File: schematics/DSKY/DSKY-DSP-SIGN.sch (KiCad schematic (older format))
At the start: 10 parts, among them U17 74LS32, U38 74LS74, U39 74LS74, U41 74LS74, U42 74LS04, U44 74LS08, U45 74LS04, U48 74LS00, U60 74LS10, U8 74LS10

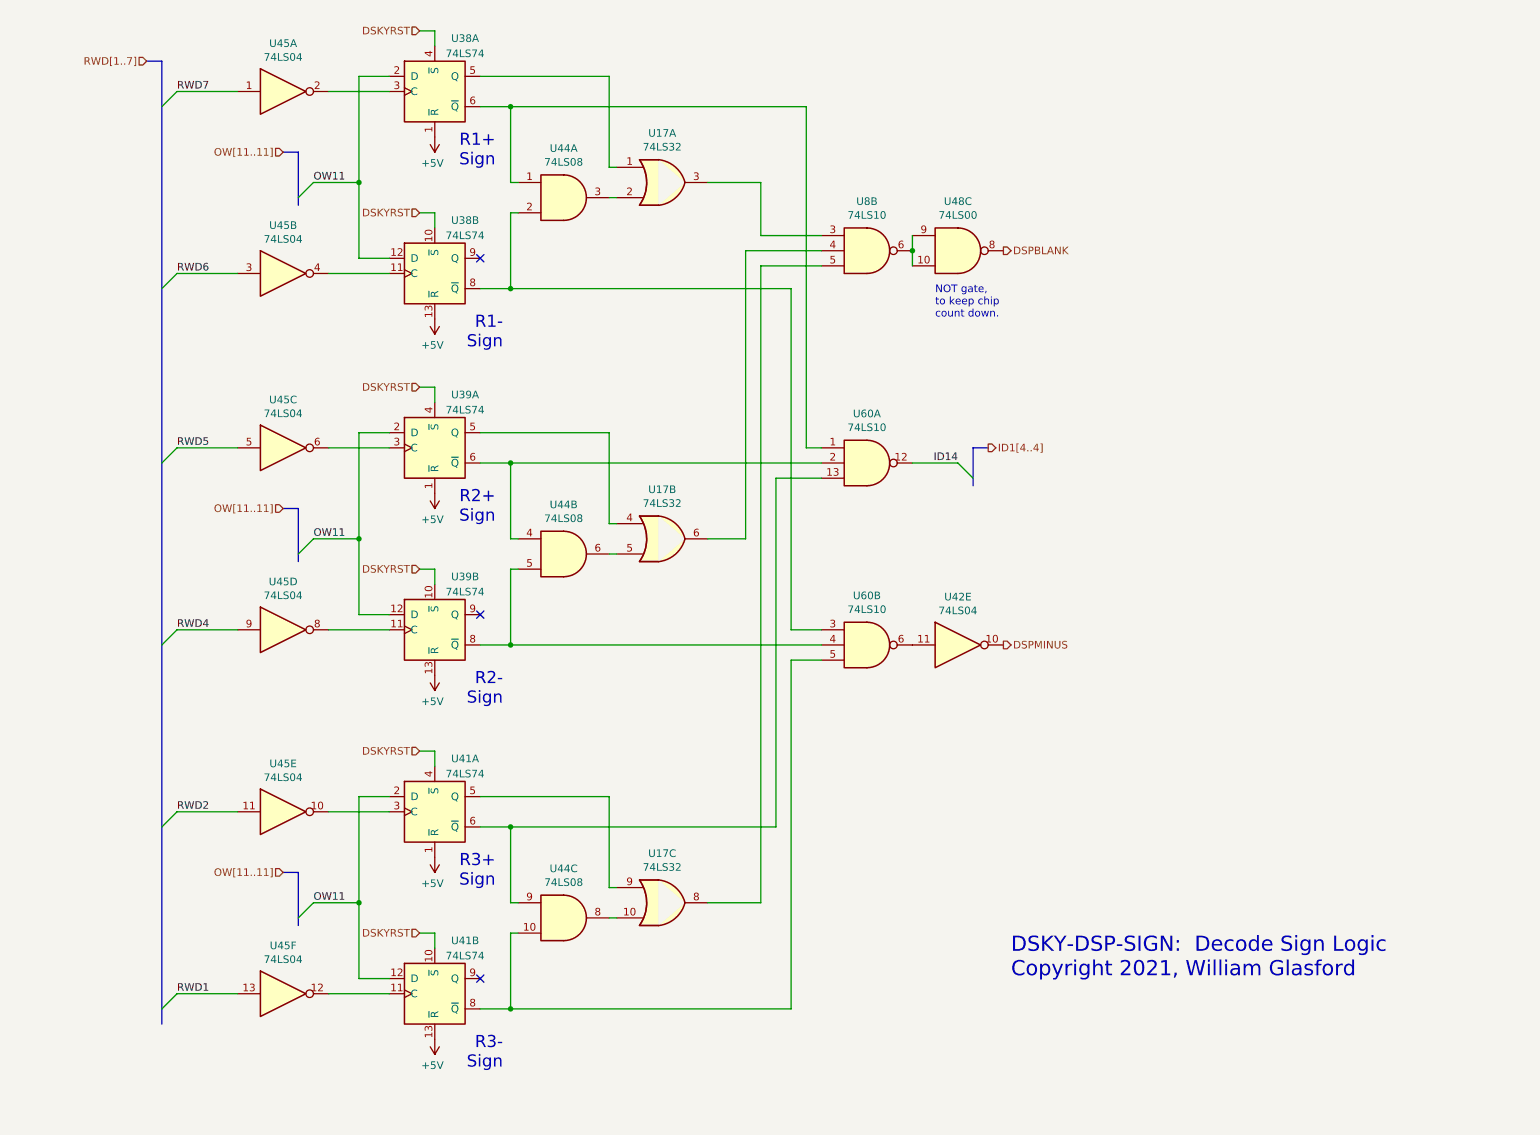
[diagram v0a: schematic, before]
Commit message: Overhauled the handling of the sign characters.
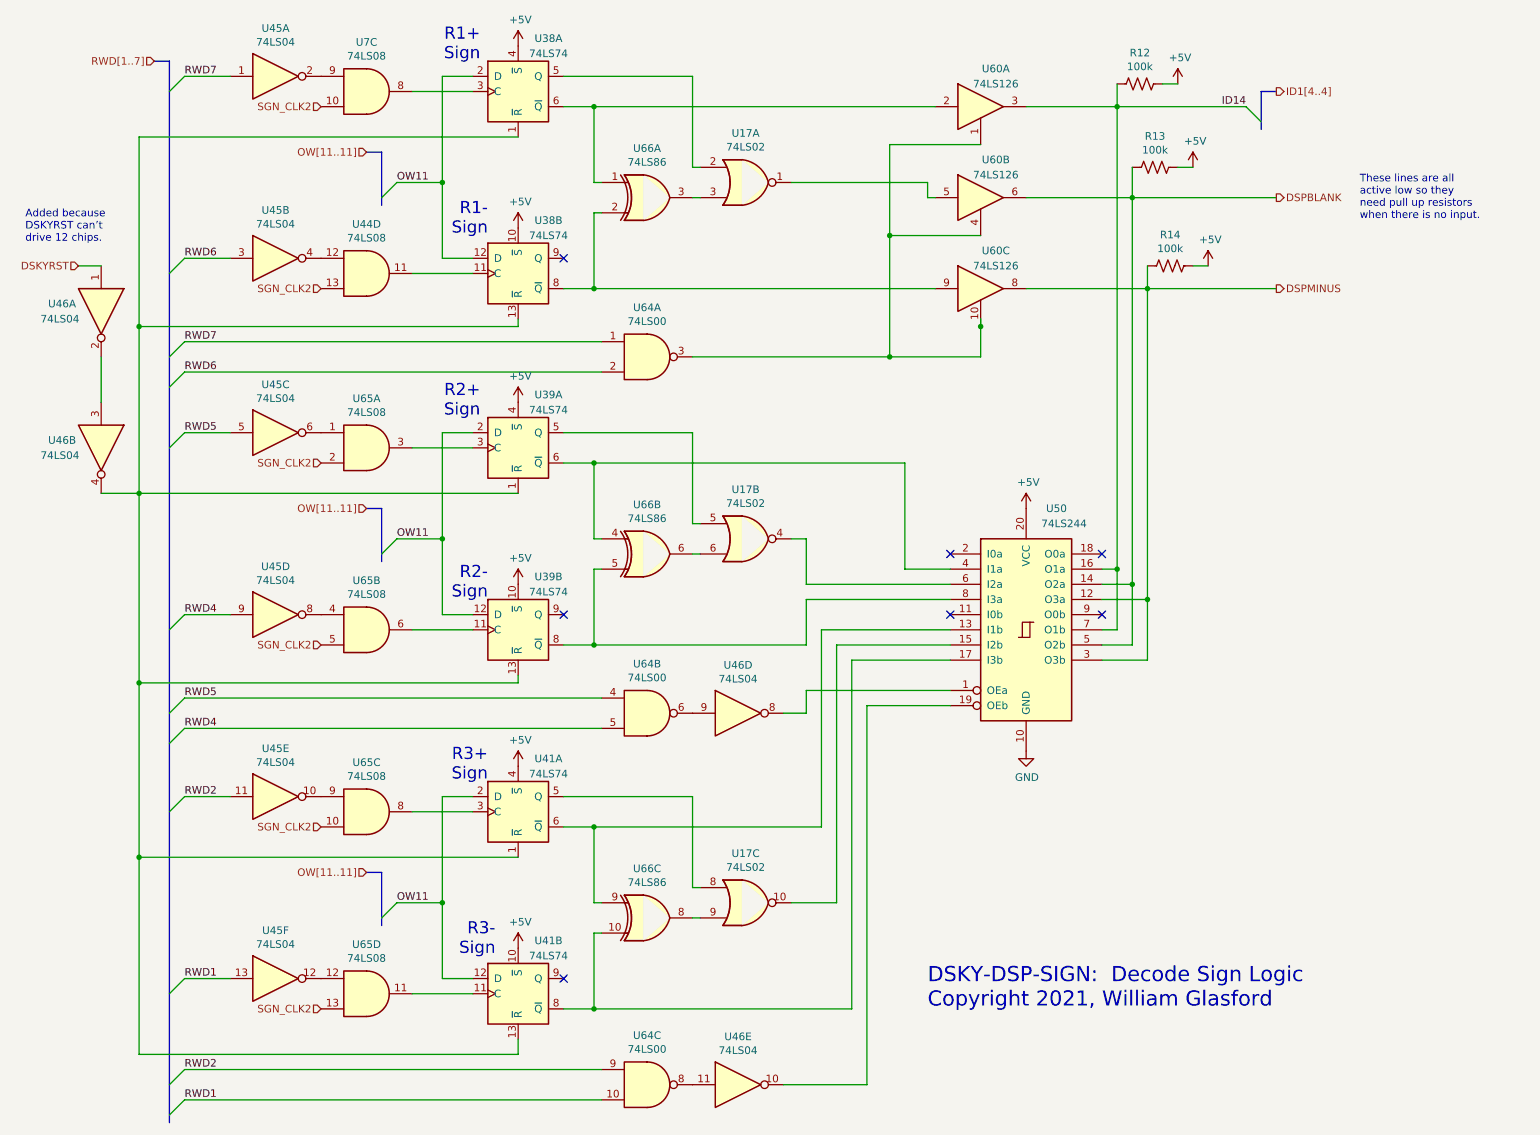
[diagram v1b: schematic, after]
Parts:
- removed U17: 74LS32, symbol 74xx:74LS32
- removed U42: 74LS04, symbol 74xx:74LS04
- removed U44: 74LS08, symbol 74xx:74LS08
- removed U48: 74LS00, symbol 74xx:74LS00
- removed U60, U8: 74LS10, symbol 74xx:74LS10
- added R12, R13, R14: 100k, symbol Device:R_US
- added U17: 74LS02, symbol 74xx:74LS02
- added U44, U65, U7: 74LS08, symbol 74xx:74LS08
- added U46: 74LS04, symbol 74xx:74LS04
- added U50: 74LS244, symbol 74xx:74LS244
- added U60: 74LS126, symbol 74xx:74LS126
- added U64: 74LS00, symbol 74xx:74LS00
- added U66: 74LS86, symbol 74xx:74LS86
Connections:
- net +5V: now also U38.10 (~S), U38.4 (~S), U39.10 (~S), U39.4 (~S), U41.10 (~S), U41.4 (~S), R12.1, R13.1, R14.1, U50.20 (VCC); no longer U38.1 (~R), U38.13 (~R), U39.1 (~R), U39.13 (~R), U41.1 (~R), U41.13 (~R)
- net DSKYRST: now also U46.1; no longer U38.10 (~S), U38.4 (~S), U39.10 (~S), U39.4 (~S), U41.10 (~S), U41.4 (~S)
- net DSPBLANK: now also R13.2, U50.14 (O2a), U50.5 (O2b), U60.6
- net DSPMINUS: now also R14.2, U50.12 (O3a), U50.3 (O3b), U60.8
- net ID14: now also R12.2, U50.16 (O1a), U50.7 (O1b), U60.3
- net RWD1: now also U64.10
- net RWD2: now also U64.9
- net RWD4: now also U64.5
- net RWD5: now also U64.4
- net RWD6: now also U64.2
- net RWD7: now also U64.1
- net at U38.3 (C): now also U7.8; no longer U45.2
- net at U38.5 (Q): now also U17.2
- net at U38.6 (~Q): now also U60.2, U66.1
- net at U38.11 (C): now also U44.11; no longer U45.4
- net at U38.8 (~Q): now also U60.9, U66.2
- net at U39.3 (C): now also U65.3; no longer U45.6
- net at U39.5 (Q): now also U17.5
- net at U39.6 (~Q): now also U50.4 (I1a), U66.4
- net at U39.11 (C): now also U65.6; no longer U45.8
- net at U39.8 (~Q): now also U50.8 (I3a), U66.5
- net at U41.3 (C): now also U65.8; no longer U45.10
- net at U41.5 (Q): now also U17.8
- net at U41.6 (~Q): now also U50.13 (I1b), U66.9
- net at U41.11 (C): now also U65.11; no longer U45.12
- net at U41.8 (~Q): now also U50.17 (I3b), U66.10
- new net: U38.1 (~R), U38.13 (~R), U39.1 (~R), U39.13 (~R), U41.1 (~R), U41.13 (~R), U46.4
- new net: U45.2, U7.9
- new net: U44.12, U45.4
- new net: U45.6, U65.1
- new net: U45.8, U65.4
- new net: U45.10, U65.9
- new net: U45.12, U65.12
- new net: U46.2, U46.3
- new net: U46.8, U50.1 (OEa)
- new net: U17.10, U50.15 (I2b)
- new net: U46.10, U50.19 (OEb)
- new net: U17.4, U50.6 (I2a)
- new net: U60.1, U60.10, U60.4, U64.3
- new net: U17.1, U60.5
- new net: U46.9, U64.6
- new net: U46.11, U64.8
- new net: U17.3, U66.3
- new net: U17.9, U66.8
- new net: U17.6, U66.6
- new net GND: U50.10 (GND)
- new net SGN_CLK2: U44.13, U65.10, U65.13, U65.2, U65.5, U7.10
- no-connect marks 3 -> 7
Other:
- note added: "Added because\nDSKYRST can’t\ndrive 12 chips."
- note added: "These lines are all \nactive low so they \nneed pull up resistors \nwhen there is no input."
- note removed: "NOT gate,\nto keep chip\ncount down."
- moved on the sheet: U38A, U38B, U39A, U39B, U41A, U41B, U45A, U45B, U45C, U45D, U45E, U45F

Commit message: Minor tweaks during implementation.
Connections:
- net DSPBLANK: now also R14.2, U50.12 (O3a), U50.3 (O3b), U60.8; no longer R13.2, U50.14 (O2a), U50.5 (O2b), U60.6
- net DSPMINUS: now also R13.2, U50.14 (O2a), U50.5 (O2b), U60.6; no longer R14.2, U50.12 (O3a), U50.3 (O3b), U60.8
- net at U38.8 (~Q), U60.9: no longer U66.2
- net at U38.9 (Q): now also U66.2
- net at U39.8 (~Q), U50.8 (I3a): no longer U66.5
- net at U39.9 (Q): now also U66.5
- net at U41.8 (~Q), U50.17 (I3b): no longer U66.10
- net at U41.9 (Q): now also U66.10
- no-connect marks 7 -> 4
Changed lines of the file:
@@
 	4950 1800 5000 1800
 Wire Wire Line
-	4100 2400 4300 2400
-Wire Wire Line
-	4300 2400 4300 1900
-Wire Wire Line
 	4300 1900 4350 1900
 Wire Wire Line
@@
 Wire Wire Line
 	4300 1700 4350 1700
-NoConn ~ 4100 2200
 Wire Wire Line
 	4100 1000 4950 1000
@@
 Text HLabel 900  2250 0    50   Input ~ 0
 DSKYRST
-Text HLabel 8800 1800 2    50   Output ~ 0
+Text HLabel 8800 2400 2    50   Output ~ 0
 DSPBLANK
 Text Notes 6500 7150 0    100  ~ 0
@@
 R1-\nSign
 Connection ~ 4300 1200
-Connection ~ 4300 2400
 Connection ~ 3300 1700
 Wire Wire Line
@@
 	4950 4150 5000 4150
 Wire Wire Line
-	4100 4750 4300 4750
-Wire Wire Line
-	4300 4750 4300 4250
-Wire Wire Line
 	4300 4250 4350 4250
 Wire Wire Line
@@
 Wire Wire Line
 	4300 4050 4350 4050
-NoConn ~ 4100 4550
 Wire Wire Line
 	4100 3350 4950 3350
@@
 Text Label 8600 1200 2    50   ~ 0
 ID14
-Text HLabel 8800 2400 2    50   Output ~ 0
+Text HLabel 8800 1800 2    50   Output ~ 0
 DSPMINUS
 Text Notes 3550 3250 2    80   ~ 0
@@
 R2-\nSign
 Connection ~ 4300 3550
-Connection ~ 4300 4750
 Connection ~ 3300 4050
 Wire Wire Line
@@
 	4950 6550 5000 6550
 Wire Wire Line
-	4100 7150 4300 7150
-Wire Wire Line
-	4300 7150 4300 6650
-Wire Wire Line
 	4300 6650 4350 6650
 Wire Wire Line
@@
 Wire Wire Line
 	4300 6450 4350 6450
-NoConn ~ 4100 6950
 Wire Wire Line
 	4100 5750 4950 5750
@@
 R3-\nSign
 Connection ~ 4300 5950
-Connection ~ 4300 7150
 Connection ~ 3300 6450
 Wire Wire Line
@@
 Wire Wire Line
 	6000 7150 6000 4850
-Wire Wire Line
-	4300 7150 6000 7150
 Wire Wire Line
 	6500 1700 5600 1700
@@
 RWD6
 Wire Wire Line
-	4300 4750 5700 4750
-Wire Wire Line
 	5700 5200 5550 5200
 Wire Wire Line
@@
 Wire Wire Line
 	4300 1200 6550 1200
-Wire Wire Line
-	4300 2400 6550 2400
 Wire Wire Line
 	6550 1800 6500 1800
@@
 Connection ~ 7750 4250
 Wire Wire Line
-	7650 4750 7850 4750
-Wire Wire Line
-	7850 4750 7850 4350
-Wire Wire Line
-	7850 4350 7650 4350
-Connection ~ 7850 4350
-Wire Wire Line
 	7150 1800 7850 1800
-Wire Wire Line
-	7650 4850 7950 4850
-Wire Wire Line
-	7950 4850 7950 4450
-Wire Wire Line
-	7950 4450 7650 4450
-Connection ~ 7950 4450
 Wire Wire Line
 	7150 2400 7950 2400
@@
 	7750 1200 7750 4250
 Connection ~ 7850 1800
-Wire Wire Line
-	7850 1800 7850 4350
 Connection ~ 7950 2400
-Wire Wire Line
-	7950 2400 7950 4450
 Text Notes 9350 1950 0    50   ~ 0
 These lines are all \nactive low so they \nneed pull up resistors \nwhen there is no input.
@@
 Wire Wire Line
 	8250 2250 8350 2250
-Wire Wire Line
-	7950 2250 7950 2400
-Wire Wire Line
-	7950 2400 8800 2400
 $Comp
 L Device:R_US R12
@@
 	1    0    0    -1
 $EndComp
+$Comp
+L 74xx:74LS02 U17
+U 1 1 624C129D
+P 5300 1700
+F 0 "U17" H 5300 2025 50  0000 C CNN
+F 1 "74LS02" H 5300 1934 50  0000 C CNN
+F 2 "" H 5300 1700 50  0001 C CNN
+F 3 "http://www.ti.com/lit/gpn/sn74ls02" H 5300 1700 50  0001 C CNN
+	1    5300 1700
+	1    0    0    -1
+$EndComp
+$Comp
+L 74xx:74LS02 U17
+U 3 1 624C69AD
+P 5300 6450
+F 0 "U17" H 5300 6775 50  0000 C CNN
+F 1 "74LS02" H 5300 6684 50  0000 C CNN
+F 2 "" H 5300 6450 50  0001 C CNN
+F 3 "http://www.ti.com/lit/gpn/sn74ls02" H 5300 6450 50  0001 C CNN
+	3    5300 6450
+	1    0    0    -1
+$EndComp
+$Comp
+L 74xx:74LS02 U17
+U 2 1 624C978D
+P 5300 4050
+F 0 "U17" H 5300 4375 50  0000 C CNN
+F 1 "74LS02" H 5300 4284 50  0000 C CNN
+F 2 "" H 5300 4050 50  0001 C CNN
+F 3 "http://www.ti.com/lit/gpn/sn74ls02" H 5300 4050 50  0001 C CNN
+	2    5300 4050
+	1    0    0    -1
+$EndComp
+$Comp
+L 74xx:74LS86 U66
+U 1 1 624D2A39
+P 4650 1800
+F 0 "U66" H 4650 2125 50  0000 C CNN
+F 1 "74LS86" H 4650 2034 50  0000 C CNN
+F 2 "" H 4650 1800 50  0001 C CNN
+F 3 "74xx/74ls86.pdf" H 4650 1800 50  0001 C CNN
+	1    4650 1800
+	1    0    0    -1
+$EndComp
+$Comp
+L 74xx:74LS86 U66
+U 2 1 624D43EF
+P 4650 4150
+F 0 "U66" H 4650 4475 50  0000 C CNN
+F 1 "74LS86" H 4650 4384 50  0000 C CNN
+F 2 "" H 4650 4150 50  0001 C CNN
+F 3 "74xx/74ls86.pdf" H 4650 4150 50  0001 C CNN
+	2    4650 4150
+	1    0    0    -1
+$EndComp
+$Comp
+L 74xx:74LS86 U66
+U 3 1 624D610B
+P 4650 6550
+F 0 "U66" H 4650 6875 50  0000 C CNN
+F 1 "74LS86" H 4650 6784 50  0000 C CNN
+F 2 "" H 4650 6550 50  0001 C CNN
+F 3 "74xx/74ls86.pdf" H 4650 6550 50  0001 C CNN
+	3    4650 6550
+	1    0    0    -1
+$EndComp
+Wire Wire Line
+	4100 4750 5700 4750
+Wire Wire Line
+	4100 2400 6550 2400
+Wire Wire Line
+	4100 7150 6000 7150
+Wire Wire Line
+	4100 6950 4300 6950
+Wire Wire Line
+	4300 6950 4300 6650
+Wire Wire Line
+	4100 4550 4300 4550
+Wire Wire Line
+	4300 4550 4300 4250
+Wire Wire Line
+	4100 2200 4300 2200
+Wire Wire Line
+	4300 2200 4300 1900
+Wire Wire Line
+	7950 2250 7950 2400
+Wire Wire Line
+	7950 2400 8800 2400
+Wire Wire Line
+	7850 4350 7650 4350
+Wire Wire Line
+	7850 1800 7850 4350
+Wire Wire Line
+	7650 4750 7850 4750
+Wire Wire Line
+	7650 4850 7950 4850
+Wire Wire Line
+	7950 4450 7650 4450
+Connection ~ 7850 4350
+Wire Wire Line
+	7850 4750 7850 4350
+Wire Wire Line
+	7950 4850 7950 4450
+Connection ~ 7950 4450
+Wire Bus Line
+	1500 900  1500 7900
 Wire Bus Line
 	2900 6250 2900 6600
@@
 Wire Bus Line
 	2900 1500 2900 1850
-Wire Bus Line
-	1500 900  1500 7900
-$Comp
-L 74xx:74LS02 U17
-U 1 1 624C129D
-P 5300 1700
-F 0 "U17" H 5300 2025 50  0000 C CNN
-F 1 "74LS02" H 5300 1934 50  0000 C CNN
-F 2 "" H 5300 1700 50  0001 C CNN
-F 3 "http://www.ti.com/lit/gpn/sn74ls02" H 5300 1700 50  0001 C CNN
-	1    5300 1700
-	1    0    0    -1
-$EndComp
-$Comp
-L 74xx:74LS02 U17
-U 3 1 624C69AD
-P 5300 6450
-F 0 "U17" H 5300 6775 50  0000 C CNN
-F 1 "74LS02" H 5300 6684 50  0000 C CNN
-F 2 "" H 5300 6450 50  0001 C CNN
-F 3 "http://www.ti.com/lit/gpn/sn74ls02" H 5300 6450 50  0001 C CNN
-	3    5300 6450
-	1    0    0    -1
-$EndComp
-$Comp
-L 74xx:74LS02 U17
-U 2 1 624C978D
-P 5300 4050
-F 0 "U17" H 5300 4375 50  0000 C CNN
-F 1 "74LS02" H 5300 4284 50  0000 C CNN
-F 2 "" H 5300 4050 50  0001 C CNN
-F 3 "http://www.ti.com/lit/gpn/sn74ls02" H 5300 4050 50  0001 C CNN
-	2    5300 4050
-	1    0    0    -1
-$EndComp
-$Comp
-L 74xx:74LS86 U66
-U 1 1 624D2A39
-P 4650 1800
-F 0 "U66" H 4650 2125 50  0000 C CNN
-F 1 "74LS86" H 4650 2034 50  0000 C CNN
-F 2 "" H 4650 1800 50  0001 C CNN
-F 3 "74xx/74ls86.pdf" H 4650 1800 50  0001 C CNN
-	1    4650 1800
-	1    0    0    -1
-$EndComp
-$Comp
-L 74xx:74LS86 U66
-U 2 1 624D43EF
-P 4650 4150
-F 0 "U66" H 4650 4475 50  0000 C CNN
-F 1 "74LS86" H 4650 4384 50  0000 C CNN
-F 2 "" H 4650 4150 50  0001 C CNN
-F 3 "74xx/74ls86.pdf" H 4650 4150 50  0001 C CNN
-	2    4650 4150
-	1    0    0    -1
-$EndComp
-$Comp
-L 74xx:74LS86 U66
-U 3 1 624D610B
-P 4650 6550
-F 0 "U66" H 4650 6875 50  0000 C CNN
-F 1 "74LS86" H 4650 6784 50  0000 C CNN
-F 2 "" H 4650 6550 50  0001 C CNN
-F 3 "74xx/74ls86.pdf" H 4650 6550 50  0001 C CNN
-	3    4650 6550
-	1    0    0    -1
-$EndComp
+Wire Wire Line
+	7950 2400 7950 4450
 $EndSCHEMATC

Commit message: Final tweaks, the DSKY is now complete!
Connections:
- net DSPBLANK: now also R13.2, U50.14 (O2a), U50.5 (O2b), U60.6; no longer R14.2, U50.12 (O3a), U50.3 (O3b), U60.8
- net DSPMINUS: now also R14.2, U50.12 (O3a), U50.3 (O3b), U60.8; no longer R13.2, U50.14 (O2a), U50.5 (O2b), U60.6
- net NRWD5: now reaches U45.6, U65.1
- net NRWD4: now reaches U45.8, U65.4
- net NRWD2: now reaches U45.10, U65.9
- net NRWD1: now reaches U45.12, U65.12
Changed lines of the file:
@@
 Text HLabel 900  2250 0    50   Input ~ 0
 DSKYRST
-Text HLabel 8800 2400 2    50   Output ~ 0
+Text HLabel 8800 1800 2    50   Output ~ 0
 DSPBLANK
 Text Notes 6500 7150 0    100  ~ 0
@@
 Text Label 8600 1200 2    50   ~ 0
 ID14
-Text HLabel 8800 1800 2    50   Output ~ 0
+Text HLabel 8800 2400 2    50   Output ~ 0
 DSPMINUS
 Text Notes 3550 3250 2    80   ~ 0
@@
 	7950 4850 7950 4450
 Connection ~ 7950 4450
-Wire Bus Line
-	1500 900  1500 7900
+Wire Wire Line
+	7950 2400 7950 4450
+Wire Wire Line
+	2500 6950 2500 6600
+Wire Wire Line
+	2500 6600 2550 6600
+Connection ~ 2500 6950
+Wire Wire Line
+	2500 5750 2500 5400
+Wire Wire Line
+	2500 5400 2550 5400
+Connection ~ 2500 5750
+Wire Wire Line
+	2500 4550 2500 4200
+Wire Wire Line
+	2500 4200 2550 4200
+Connection ~ 2500 4550
+Wire Wire Line
+	2500 3350 2500 3050
+Wire Wire Line
+	2500 3050 2550 3050
+Connection ~ 2500 3350
+Text HLabel 2550 3050 2    50   Output ~ 0
+NRWD5
+Text HLabel 2550 4200 2    50   Output ~ 0
+NRWD4
+Text HLabel 2550 5400 2    50   Output ~ 0
+NRWD2
+Text HLabel 2550 6600 2    50   Output ~ 0
+NRWD1
 Wire Bus Line
 	2900 6250 2900 6600
@@
 Wire Bus Line
 	2900 1500 2900 1850
-Wire Wire Line
-	7950 2400 7950 4450
+Wire Bus Line
+	1500 900  1500 7900
 $EndSCHEMATC
